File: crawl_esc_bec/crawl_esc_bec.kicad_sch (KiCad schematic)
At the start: 42 parts, among them IC1 L78M06ABDT-TR, IC2 LM25085AMY, IC3 LMR62014XMFE/NOPB

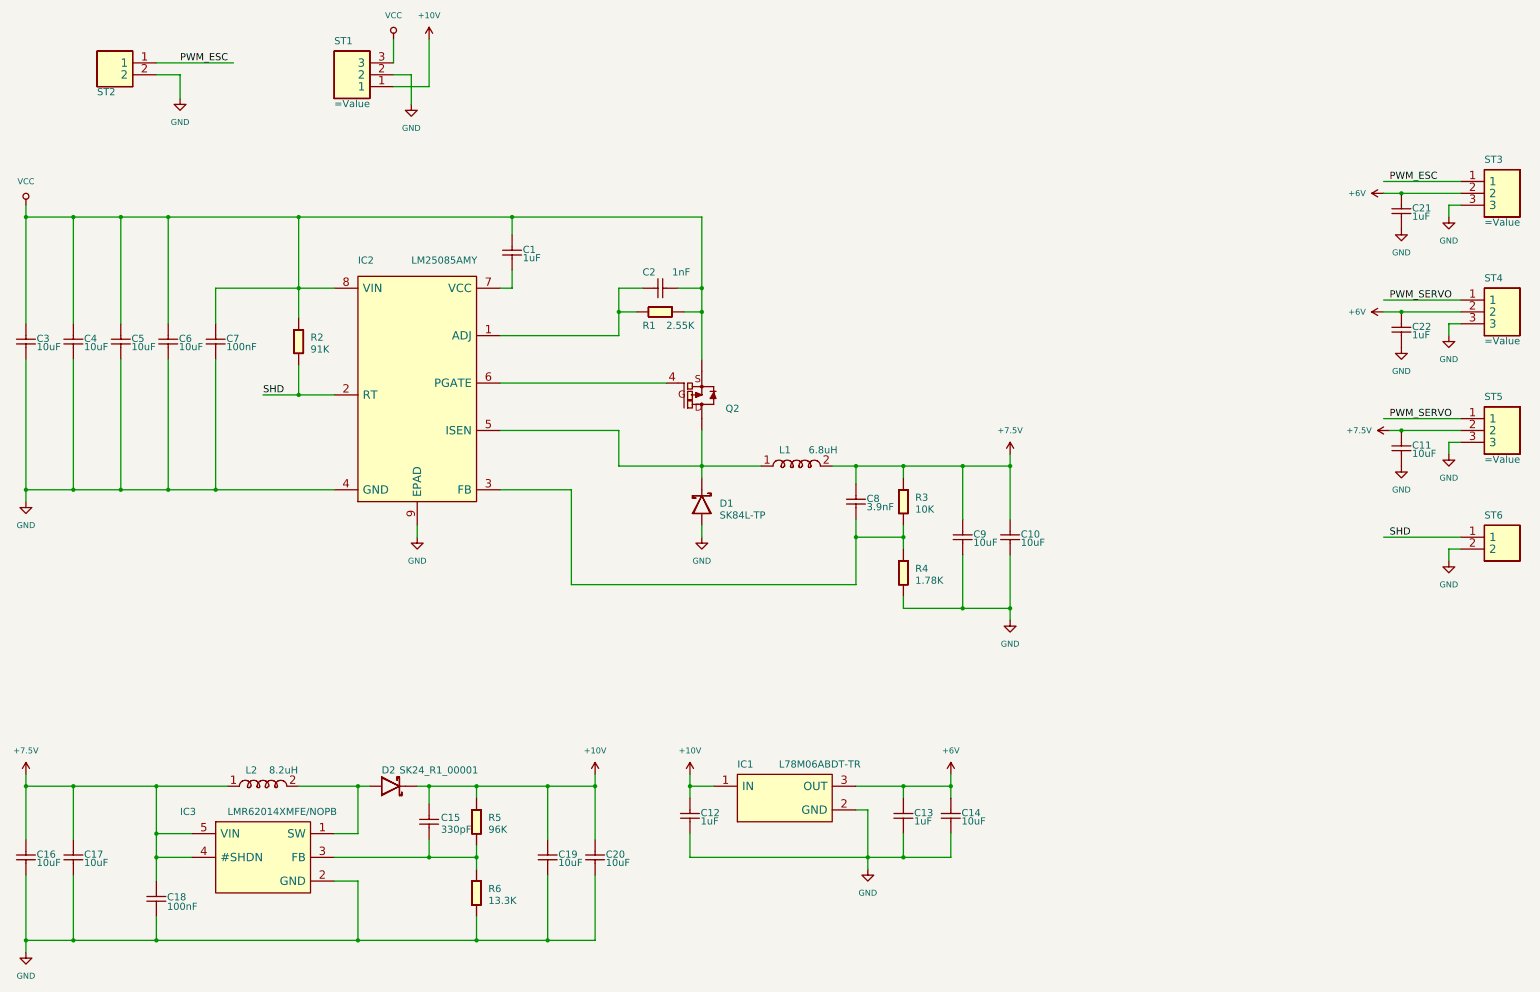
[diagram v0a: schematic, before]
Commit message: change stepup isens layout
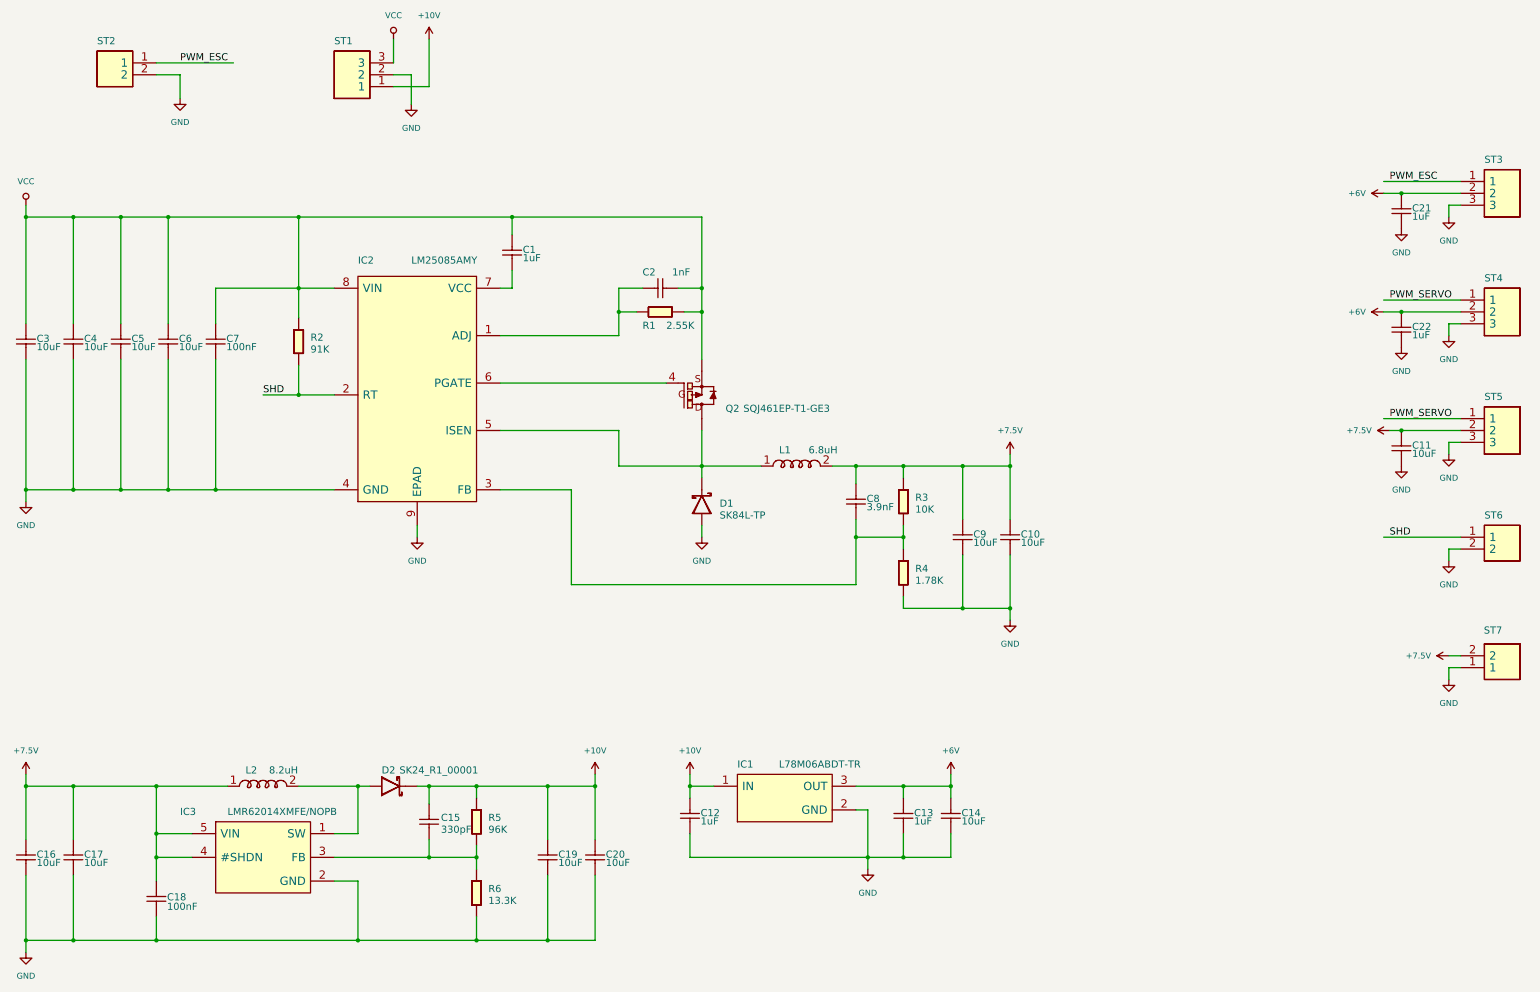
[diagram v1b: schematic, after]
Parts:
- added ST7: ~, Super_Lib_V1_0.IntLib:STL2X1, symbol testnoibec_bec-rescue:Header_2X1-
- Q2: value (none) -> SQJ461EP-T1-GE3
- ST1: footprint (none) -> test.PcbLib:STL3X1
- ST2, ST6: footprint (none) -> Super_Lib_V1_0.IntLib:STL2X1
- ST5: value =Value -> (none)
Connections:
- net +7.5V: now also ST7.2
- net GND: now also ST7.1
